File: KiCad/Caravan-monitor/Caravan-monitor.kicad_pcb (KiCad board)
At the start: 2 copper layers, 40 parts, among them IC1 TPS54302DDCR, IC2 STM32L011F4P6TR, IC3 INA500CIDBVR, IC4 TPS54302DDCR, J1 Conn_ARM_JTAG_SWD_20, J2 PJ-059A

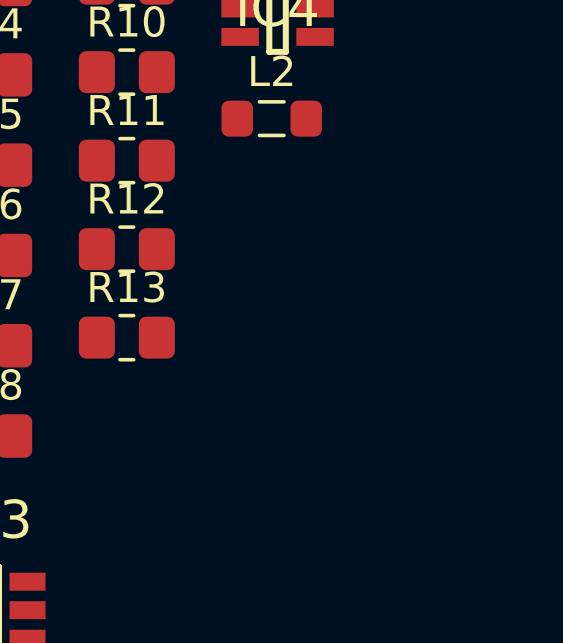
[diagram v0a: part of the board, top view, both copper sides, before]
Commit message: Temperature monitoring schematics
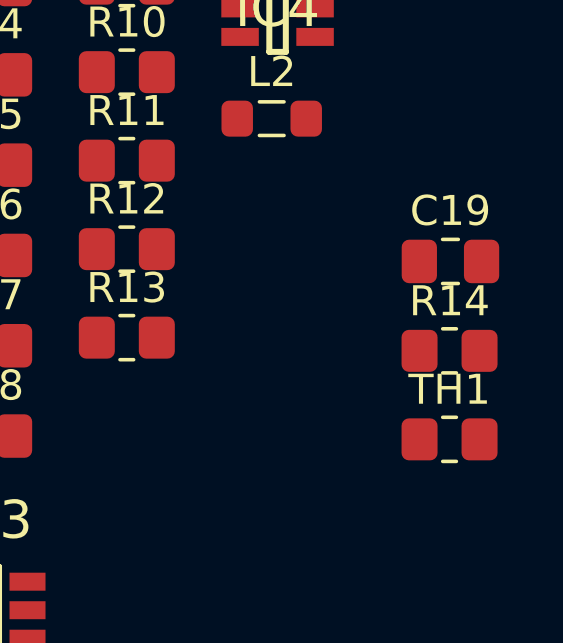
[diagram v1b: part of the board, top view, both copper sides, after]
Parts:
- added C19: 100n, Capacitor_SMD:C_0805_2012Metric_Pad1.18x1.45mm_HandSolder, F.Cu at (125.0, 40.6)
- added R14: 47k, Resistor_SMD:R_0805_2012Metric_Pad1.20x1.40mm_HandSolder, F.Cu at (125.0, 43.5)
- added TH1: Thermistor_NTC, Resistor_SMD:R_0805_2012Metric_Pad1.20x1.40mm_HandSolder, F.Cu at (125.0, 46.5)

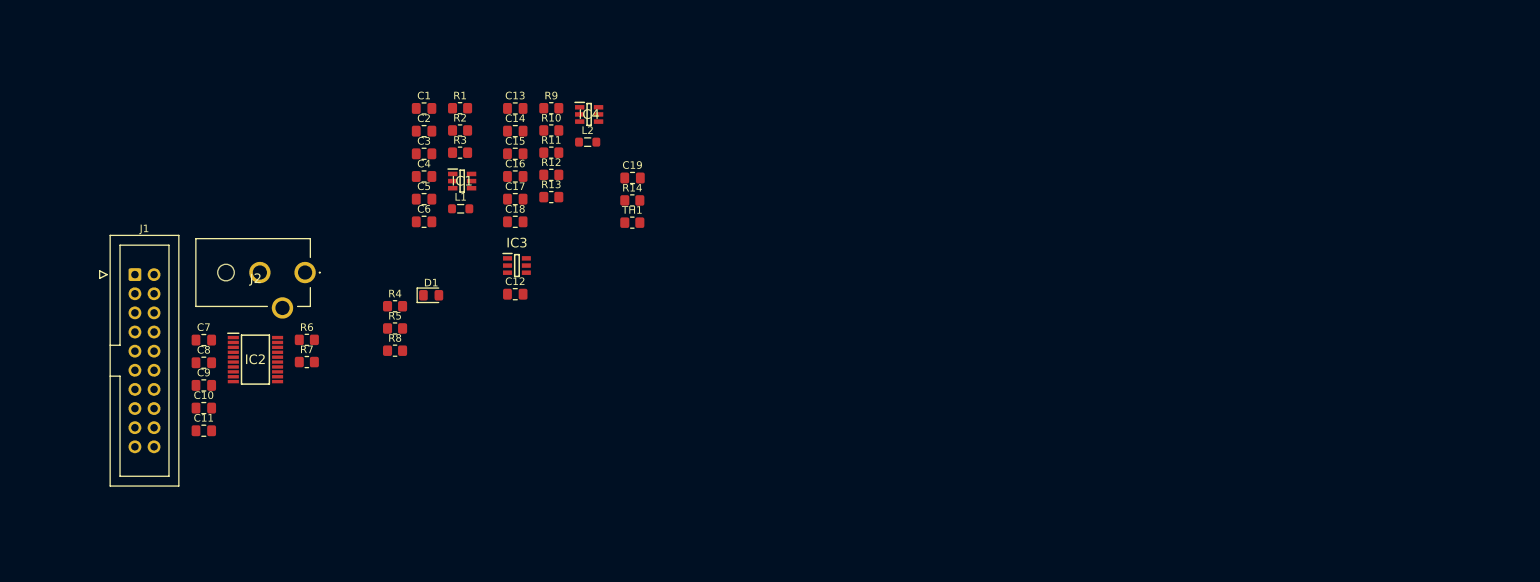
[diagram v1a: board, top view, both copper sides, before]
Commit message: Display schematics
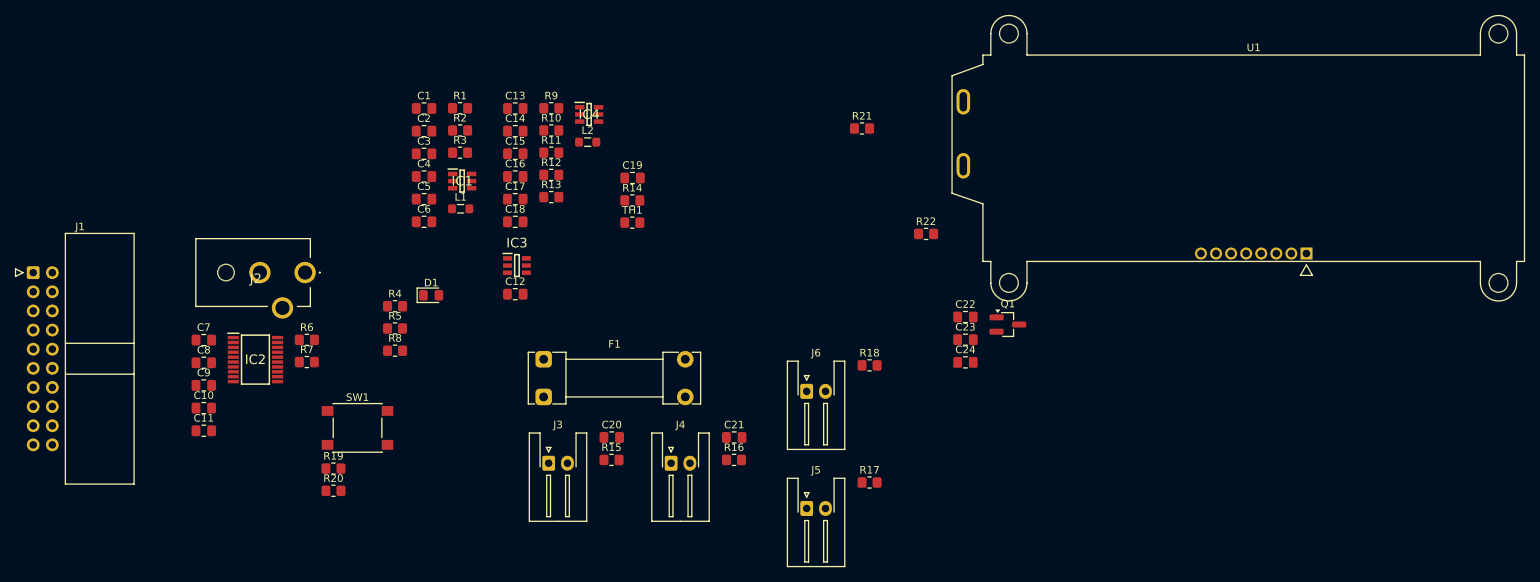
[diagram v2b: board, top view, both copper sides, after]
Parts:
- added C20: 100n, Capacitor_SMD:C_0805_2012Metric_Pad1.18x1.45mm_HandSolder, F.Cu at (122.3, 75.0)
- added C21: 100n, Capacitor_SMD:C_0805_2012Metric_Pad1.18x1.45mm_HandSolder, F.Cu at (138.5, 75.0)
- added C22: 100n, Capacitor_SMD:C_0805_2012Metric_Pad1.18x1.45mm_HandSolder, F.Cu at (169.2, 59.0)
- added C23: 0.47µ, Capacitor_SMD:C_0805_2012Metric_Pad1.18x1.45mm_HandSolder, F.Cu at (169.2, 62.0)
- added C24: 100n, Capacitor_SMD:C_0805_2012Metric_Pad1.18x1.45mm_HandSolder, F.Cu at (169.2, 65.0)
- added F1: 500mA, Fuse:Fuseholder_Clip-5x20mm_Littelfuse_111_Lateral_P18.80x5.00mm_D1.17mm_Horizontal, F.Cu at (113.2, 64.6)
- added J3: Outdoor temp, Connector_JST:JST_XH_S2B-XH-A-1_1x02_P2.50mm_Horizontal, F.Cu at (113.9, 78.4)
- added J4: Coolant temp, Connector_JST:JST_XH_S2B-XH-A-1_1x02_P2.50mm_Horizontal, F.Cu at (130.2, 78.4)
- added J5: Water tank 1, Connector_JST:JST_XH_S2B-XH-A-1_1x02_P2.50mm_Horizontal, F.Cu at (148.2, 84.5)
- added J6: Water tank 2, Connector_JST:JST_XH_S2B-XH-A-1_1x02_P2.50mm_Horizontal, F.Cu at (148.2, 68.9)
- added Q1: 2N7002, Package_TO_SOT_SMD:SOT-23_Handsoldering, F.Cu at (174.9, 60.0)
- added R15: 47k, Resistor_SMD:R_0805_2012Metric_Pad1.20x1.40mm_HandSolder, F.Cu at (122.2, 78.0)
- added R16: 10k, Resistor_SMD:R_0805_2012Metric_Pad1.20x1.40mm_HandSolder, F.Cu at (138.5, 78.0)
- added R17: 10k, Resistor_SMD:R_0805_2012Metric_Pad1.20x1.40mm_HandSolder, F.Cu at (156.5, 81.0)
- added R18: 10k, Resistor_SMD:R_0805_2012Metric_Pad1.20x1.40mm_HandSolder, F.Cu at (156.5, 65.5)
- added R19: 4.7k, Resistor_SMD:R_0805_2012Metric_Pad1.20x1.40mm_HandSolder, F.Cu at (85.3, 79.2)
- added R20: 4.7k, Resistor_SMD:R_0805_2012Metric_Pad1.20x1.40mm_HandSolder, F.Cu at (85.3, 82.1)
- added R21: 10R, Resistor_SMD:R_0805_2012Metric_Pad1.20x1.40mm_HandSolder, F.Cu at (155.5, 34.0)
- added R22: 1k, Resistor_SMD:R_0805_2012Metric_Pad1.20x1.40mm_HandSolder, F.Cu at (164.0, 48.0)
- added SW1: SW_SPST, Button_Switch_SMD:SW_SPST_PTS645, F.Cu at (88.5, 73.8)
- added U1: NHD-C0220BIZ, Display:NHD-C0220BiZ, F.Cu at (207.5, 34.7)
- J1: footprint Connector_IDC:IDC-Header_2x10_P2.54mm_Vertical -> Connector_IDC:IDC-Header_2x10_P2.54mm_Horizontal
- J2: value PJ-059A -> 8-28V input
- moved J1 13.5 mm to (45.5, 53.1)
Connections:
- C19 pad 1: /Indoor temperature/Out -> IndoorTemp
- IC2 pad 10: unconnected-(IC2-PA4-Pad10) -> WaterTank1
- IC2 pad 11: unconnected-(IC2-PA5-Pad11) -> WaterTank2
- IC2 pad 12: unconnected-(IC2-PA6-Pad12) -> DisplayBacklight
- IC2 pad 14: unconnected-(IC2-PB1-Pad14) -> DisplayReset
- IC2 pad 17: unconnected-(IC2-PA9-Pad17) -> SCL
- IC2 pad 18: unconnected-(IC2-PA10-Pad18) -> SDA
- IC2 pad 7: unconnected-(IC2-PA1-Pad7) -> IndoorTemp
- IC2 pad 8: unconnected-(IC2-PA2-Pad8) -> OutdoorTemp
- IC2 pad 9: unconnected-(IC2-PA3-Pad9) -> CoolantTemp
- J2 pad 3: Battery+ -> Net-(F1-Pad2)
- R14 pad 1: /Indoor temperature/3.3V -> 3.3V
- R14 pad 2: /Indoor temperature/Out -> IndoorTemp
- TH1 pad 1: /Indoor temperature/Out -> IndoorTemp

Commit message: Schematics done
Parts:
- removed IC2: STM32L011F4P6TR, SamacSys_Parts:SOP65P640X120-20N
- added C25: 100n, Capacitor_SMD:C_0402_1005Metric_Pad0.74x0.62mm_HandSolder, F.Cu at (69.2, 92.0)
- added C26: 1µ, Capacitor_SMD:C_0402_1005Metric_Pad0.74x0.62mm_HandSolder, F.Cu at (193.7, 71.0)
- added C27: 100n, Capacitor_SMD:C_0402_1005Metric_Pad0.74x0.62mm_HandSolder, F.Cu at (193.7, 74.0)
- added C28: 100n, Capacitor_SMD:C_0402_1005Metric_Pad0.74x0.62mm_HandSolder, F.Cu at (193.7, 77.0)
- added C29: 10p, Capacitor_SMD:C_0402_1005Metric_Pad0.74x0.62mm_HandSolder, F.Cu at (193.7, 80.0)
- added C30: 10p, Capacitor_SMD:C_0402_1005Metric_Pad0.74x0.62mm_HandSolder, F.Cu at (193.7, 83.0)
- added D2: WT1_LED, LED_SMD:LED_0402_1005Metric_Pad0.77x0.64mm_HandSolder, F.Cu at (138.4, 86.0)
- added D3: WT2_LED, LED_SMD:LED_0402_1005Metric_Pad0.77x0.64mm_HandSolder, F.Cu at (138.4, 88.0)
- added FB1: 120R, Inductor_SMD:L_0402_1005Metric_Pad0.77x0.64mm_HandSolder, F.Cu at (198.4, 82.3)
- added J8: STM32 Pins, Connector_PinHeader_2.54mm:PinHeader_2x13_P2.54mm_Horizontal, F.Cu at (148.2, 103.8)
- added R23: 10k, Resistor_SMD:R_0402_1005Metric_Pad0.72x0.64mm_HandSolder, F.Cu at (74.0, 92.0)
- added R24: 1k, Resistor_SMD:R_0402_1005Metric_Pad0.72x0.64mm_HandSolder, F.Cu at (182.5, 84.0)
- added R25: 1k, Resistor_SMD:R_0402_1005Metric_Pad0.72x0.64mm_HandSolder, F.Cu at (134.9, 88.0)
- added SW2: SW_USER, Button_Switch_SMD:SW_SPST_PTS645, F.Cu at (72.4, 86.6)
- added SW3: SW_DPDT_x2, Button_Switch_THT:SW_E-Switch_EG2219_DPDT_Angled, F.Cu at (138.5, 46.2)
- added U2: STM32L010C6Tx, Package_QFP:LQFP-48_7x7mm_P0.5mm, F.Cu at (201.8, 75.2)
- C1, C10, C11, C12, C13, C14, C15, C16, C17, C18, C19, C2, C20, C21, C22, C23, C24, C3, C4, C5, C6, C7, C9: footprint Capacitor_SMD:C_0805_2012Metric_Pad1.18x1.45mm_HandSolder -> Capacitor_SMD:C_0402_1005Metric_Pad0.74x0.62mm_HandSolder
- C8: value 100n -> 10n; footprint Capacitor_SMD:C_0805_2012Metric_Pad1.18x1.45mm_HandSolder -> Capacitor_SMD:C_0402_1005Metric_Pad0.74x0.62mm_HandSolder
- D1: footprint LED_SMD:LED_0805_2012Metric_Pad1.15x1.40mm_HandSolder -> LED_SMD:LED_0402_1005Metric_Pad0.77x0.64mm_HandSolder
- R1, R10, R11, R12, R13, R14, R15, R16, R17, R18, R19, R2, R20, R21, R22, R3, R4, R5, R6, R7, R8, R9, TH1: footprint Resistor_SMD:R_0805_2012Metric_Pad1.20x1.40mm_HandSolder -> Resistor_SMD:R_0402_1005Metric_Pad0.72x0.64mm_HandSolder
- SW1: value SW_SPST -> SW_RESET
- moved J5 59.8 mm to (93.2, 108.2)
- moved J6 58.9 mm to (104.2, 108.2)
- moved J4 57.6 mm to (80.8, 108.2)
- moved J3 54.0 mm to (68.8, 108.2)
- moved R8 47.1 mm to (134.9, 86.0)
- moved J1 29.3 mm to (54.5, 81.0), turned to 180 degrees
- moved J2 27.8 mm to (56.0, 42.2)
- moved U1 15.7 mm to (223.0, 37.2)
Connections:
- net 5V renamed +5V
- C1 pad 1: Battery+ -> +BATT
- C1 pad 2: Battery- -> GND
- C10 pad 1: 3.3V -> +3.3VA
- C10 pad 2: Battery- -> GND
- C11 pad 1: 3.3V -> +3.3V
- C11 pad 2: Battery- -> GND
- C12 pad 2: Battery- -> GND
- C13 pad 1: Battery+ -> +BATT
- C13 pad 2: Battery- -> GND
- C14 pad 1: Battery+ -> +BATT
- C14 pad 2: Battery- -> GND
- C16 pad 2: Battery- -> GND
- C17 pad 2: Battery- -> GND
- C19 pad 2: Battery- -> GND
- C2 pad 1: Battery+ -> +BATT
- C2 pad 2: Battery- -> GND
- C20 pad 2: Battery- -> GND
- C21 pad 2: Battery- -> GND
- C23 pad 1: Battery- -> GND
- C24 pad 1: 3.3V -> +3.3V
- C24 pad 2: Battery- -> GND
- C4 pad 1: 3.3V -> +3.3V
- C4 pad 2: Battery- -> GND
- C5 pad 1: 3.3V -> +3.3V
- C5 pad 2: Battery- -> GND
- C7 pad 1: 3.3V -> +3.3V
- C7 pad 2: Battery- -> GND
- C8 pad 1: 3.3V -> +3.3VA
- C8 pad 2: Battery- -> GND
- C9 pad 1: Battery- -> GND
- D1 pad 1: Battery- -> Net-(D1-K)
- D1 pad 2: Net-(D1-A) -> +3.3V
- F1 pad 1: Battery+ -> Net-(SW3A-B)
- IC1 pad 1: Battery- -> GND
- IC1 pad 3: Battery+ -> +BATT
- IC3 pad 2: Battery- -> GND
- IC3 pad 3: Battery+ -> +BATT
- IC3 pad 4: Battery- -> GND
- IC3 pad 5: Battery- -> GND
- IC4 pad 1: Battery- -> GND
- IC4 pad 3: Battery+ -> +BATT
- J1 pad 10: Battery- -> GND
- J1 pad 12: Battery- -> GND
- J1 pad 14: Battery- -> GND
- J1 pad 16: Battery- -> GND
- J1 pad 18: Battery- -> GND
- J1 pad 2: 3.3V -> +3.3V
- J1 pad 20: Battery- -> GND
- J1 pad 4: Battery- -> GND
- J1 pad 6: Battery- -> GND
- J1 pad 8: Battery- -> GND
- J2 pad 2: Battery- -> GND
- J3 pad 2: Battery- -> GND
- J4 pad 2: Battery- -> GND
- J5 pad 2: Battery- -> GND
- J6 pad 2: Battery- -> GND
- L1 pad 2: 3.3V -> +3.3V
- Q1 pad 2: Battery- -> GND
- R1 pad 1: Battery+ -> +BATT
- R10 pad 2: Battery- -> GND
- R12 pad 1: Battery+ -> +BATT
- R13 pad 2: Battery- -> GND
- R14 pad 1: 3.3V -> +3.3V
- R15 pad 1: 3.3V -> +3.3V
- R16 pad 1: 3.3V -> +3.3V
- R17 pad 1: 3.3V -> +3.3V
- R18 pad 1: 3.3V -> +3.3V
- R19 pad 1: 3.3V -> +3.3V
- R19 pad 2: SDA -> SCL
- R2 pad 2: Battery- -> GND
- R20 pad 1: 3.3V -> +3.3V
- R20 pad 2: SCL -> SDA
- R21 pad 1: 3.3V -> +3.3V
- R3 pad 1: 3.3V -> +3.3V
- R5 pad 2: Battery- -> GND
- R6 pad 1: Battery- -> GND
- R6 pad 2: Net-(IC2-PB9-BOOT0) -> /BOOT0
- R7 pad 1: 3.3V -> +3.3V
- R8 pad 1: 3.3V -> Net-(D3-K)
- R8 pad 2: Net-(D1-A) -> GND
- SW1 pad 2: Battery- -> GND
- TH1 pad 2: Battery- -> GND
- U1 pad 4: Battery- -> GND
- U1 pad 5: 3.3V -> +3.3V
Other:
- board text added: "8-28V"
- board text added: "ST-LINK"

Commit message: 3.3V and 5V PSU layout done
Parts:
- removed R7: 10k, Resistor_SMD:R_0402_1005Metric_Pad0.72x0.64mm_HandSolder
- removed SW1: SW_RESET, Button_Switch_SMD:SW_SPST_PTS645
- moved C11 144.0 mm to (203.9, 122.0)
- moved C8 144.0 mm to (203.9, 113.0)
- moved C9 144.0 mm to (203.9, 116.0)
- moved C10 144.0 mm to (203.9, 119.0)
- moved C7 144.0 mm to (203.9, 110.0)
- moved R24 132.7 mm to (61.5, 29.5), turned to -90 degrees
- moved C12 129.3 mm to (232.0, 97.3)
- moved C19 129.3 mm to (247.6, 81.8)
- moved IC3 129.3 mm to (232.2, 93.5)
- moved R14 129.3 mm to (247.6, 84.8)
- moved R21 129.3 mm to (278.1, 75.3)
- moved TH1 129.3 mm to (247.6, 87.8)
- moved U2 129.3 mm to (72.5, 77.5)
- moved C23 110.0 mm to (270.7, 104.5)
- moved C24 110.0 mm to (270.7, 107.5)
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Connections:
- C9 pad 2: NRST -> /NRST
- J1 pad 15: NRST -> unconnected-(J1-~{SRST}-Pad15)
- U2 pad 7: NRST -> /NRST
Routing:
- net GND: track 0.00 -> 53.9 mm, vias 0 -> 10
- net +BATT: track 0.00 -> 30.5 mm
- net Net-(C6-Pad1): track 0.00 -> 19.3 mm
- net Net-(SW3A-B): track 0.00 -> 17.7 mm
- net Net-(F1-Pad2): track 0.00 -> 13.5 mm
- net Net-(IC4-EN): track 0.00 -> 11.8 mm
- net Net-(IC1-EN): track 0.00 -> 11.5 mm
- net Net-(IC4-SW): track 0.00 -> 8.20 mm, vias 0 -> 2
- net Net-(IC1-SW): track 0.00 -> 7.89 mm, vias 0 -> 2
- net Net-(IC1-BOOT): track 0.00 -> 7.50 mm, vias 0 -> 2
- net +3.3V: track 0.00 -> 7.43 mm
- net Net-(IC4-BOOT): track 0.00 -> 6.86 mm, vias 0 -> 2
- net Net-(IC1-FB): track 0.00 -> 6.79 mm
- net +5V: track 0.00 -> 6.73 mm
- net Net-(IC4-FB): track 0.00 -> 6.31 mm
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
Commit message: PCB Designed
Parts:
- removed C13: 10µ, Capacitor_SMD:C_0402_1005Metric_Pad0.74x0.62mm_HandSolder
- removed C14, C15: 0.1µ, Capacitor_SMD:C_0402_1005Metric_Pad0.74x0.62mm_HandSolder
- removed C16, C17: 22µ, Capacitor_SMD:C_0402_1005Metric_Pad0.74x0.62mm_HandSolder
- removed C18: 75p, Capacitor_SMD:C_0402_1005Metric_Pad0.74x0.62mm_HandSolder
- removed IC4: TPS54302DDCR, SamacSys_Parts:SOT95P280X110-6N
- removed J8: STM32 Pins, Connector_PinHeader_2.54mm:PinHeader_2x13_P2.54mm_Horizontal
- removed L2: 10µ, Inductor_SMD:L_0805_2012Metric_Pad1.05x1.20mm_HandSolder
- removed R10: 13.3k, Resistor_SMD:R_0402_1005Metric_Pad0.72x0.64mm_HandSolder
- removed R11: 49.9, Resistor_SMD:R_0402_1005Metric_Pad0.72x0.64mm_HandSolder
- removed R12: 511k, Resistor_SMD:R_0402_1005Metric_Pad0.72x0.64mm_HandSolder
- removed R13: 105k, Resistor_SMD:R_0402_1005Metric_Pad0.72x0.64mm_HandSolder
- removed R9: 100k, Resistor_SMD:R_0402_1005Metric_Pad0.72x0.64mm_HandSolder
- added Y1: 16MHz, Package_LGA:VLGA-4_2x2.5mm_P1.65mm, F.Cu at (64.6, 55.2)
- C22, C23, C24, R21: moved to B.Cu
- moved IC3 193.4 mm to (43.8, 50.0)
- moved C12 193.1 mm to (45.5, 47.5)
- moved R17 181.3 mm to (77.6, 106.2)
- moved D2 175.5 mm to (76.5, 64.5), turned to 180 degrees
- moved R21 172.7 mm to (105.5, 81.1), turned to 90 degrees
- moved D3 172.6 mm to (76.5, 75.0), turned to 180 degrees
- moved R16 172.0 mm to (68.6, 106.2)
- moved R18 171.7 mm to (86.3, 106.2)
- moved C23 171.2 mm to (101.0, 82.1), turned to 90 degrees
- moved R25 170.8 mm to (78.9, 64.5)
- moved C21 169.5 mm to (70.9, 106.0)
- moved C24 168.0 mm to (104.5, 83.4), turned to -90 degrees
- moved R8 166.3 mm to (79.0, 75.0)
- moved R14 165.4 mm to (87.0, 45.0)
- moved R15 164.8 mm to (59.6, 106.2)
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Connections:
- net Net-(Q1-D) renamed /Display/BL_Cathode
- net Net-(U1-A) renamed /Display/BL_Anode
- C12 pad 1: +5V -> +3.3V
- IC3 pad 6: +5V -> +3.3V
- U2 pad 1: PC0 -> unconnected-(U2-PC0-Pad1)
- U2 pad 12: Net-(J8-Pin_3) -> unconnected-(U2-PA2-Pad12)
- U2 pad 13: Net-(J8-Pin_4) -> unconnected-(U2-PA3-Pad13)
- U2 pad 14: Net-(J8-Pin_5) -> unconnected-(U2-PA4-Pad14)
- U2 pad 15: Net-(J8-Pin_6) -> unconnected-(U2-PA5-Pad15)
- U2 pad 16: Net-(J8-Pin_7) -> unconnected-(U2-PA6-Pad16)
- U2 pad 17: Net-(J8-Pin_8) -> unconnected-(U2-PA7-Pad17)
- U2 pad 18: PB0 -> unconnected-(U2-PB0-Pad18)
- U2 pad 19: PB1 -> unconnected-(U2-PB1-Pad19)
- U2 pad 2: PC13 -> unconnected-(U2-PC13-Pad2)
- U2 pad 20: PB2 -> unconnected-(U2-PB2-Pad20)
- U2 pad 29: Net-(J8-Pin_9) -> unconnected-(U2-PA8-Pad29)
- U2 pad 3: PC14 -> unconnected-(U2-PC14-Pad3)
- U2 pad 32: Net-(J8-Pin_10) -> unconnected-(U2-PA11-Pad32)
- U2 pad 33: Net-(J8-Pin_11) -> unconnected-(U2-PA12-Pad33)
- U2 pad 38: Net-(J8-Pin_12) -> unconnected-(U2-PA15-Pad38)
- U2 pad 39: PB3 -> unconnected-(U2-PB3-Pad39)
- U2 pad 4: PC15 -> unconnected-(U2-PC15-Pad4)
- U2 pad 40: PB4 -> unconnected-(U2-PB4-Pad40)
- U2 pad 41: PB5 -> unconnected-(U2-PB5-Pad41)
- U2 pad 42: PB6 -> unconnected-(U2-PB6-Pad42)
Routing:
- net GND: track 53.9 -> 396.1 mm, vias 10 -> 7
- net +3.3V: track 7.43 -> 263.4 mm
- net WaterTank2: track 0.00 -> 98.6 mm, vias 0 -> 1
- net OutdoorTemp: track 0.00 -> 70.6 mm, vias 0 -> 1
- net CoolantTemp: track 0.00 -> 67.7 mm, vias 0 -> 1
- net SWDIO: track 0.00 -> 67.2 mm, vias 0 -> 1
- net SWCLK: track 0.00 -> 65.4 mm, vias 0 -> 1
- net WaterTank1: track 0.00 -> 64.3 mm, vias 0 -> 1
- net DisplayReset: track 0.00 -> 59.6 mm, vias 0 -> 1
- net SDA: track 0.00 -> 59.4 mm, vias 0 -> 3
- net SCL: track 0.00 -> 55.0 mm, vias 0 -> 1
- net Net-(SW2-B): track 0.00 -> 46.8 mm, vias 0 -> 2
- net /Display/BL_Cathode: track 0.00 -> 39.9 mm
- net /Display/BL_Anode: track 0.00 -> 39.3 mm
- net BatteryVoltage: track 0.00 -> 37.8 mm, vias 0 -> 2
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- added copper zone on B.Cu, net GND
- added copper zone on F.Cu, net GND
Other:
- board outline added: 102.5 x 80 mm
- board text added: "12V Battery"
- board text added: "500mA"
- board text added: "Coolant temp"
- board text added: "Outdoor temp"
- board text added: "Water tank 1"
- board text added: "Water tank 1 LED"
- board text added: "Water tank 2"
- board text added: "Water tank 2 LED"
- board text removed: "8-28V"

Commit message: Version 0.1 complete
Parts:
- removed C29, C30: 10p, Capacitor_SMD:C_0402_1005Metric_Pad0.74x0.62mm_HandSolder
- removed Y1: 16MHz, Package_LGA:VLGA-4_2x2.5mm_P1.65mm
- added G***: LOGO, LOGO, B.Cu at (113.0, 106.5)
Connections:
- U2 pad 5: /OSC_IN -> unconnected-(U2-PH0-Pad5)
- U2 pad 6: /OSC_OUT -> unconnected-(U2-PH1-Pad6)
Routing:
- net GND: track 396.1 -> 381.1 mm
- net /OSC_IN: track 9.45 -> 0.00 mm
- net /OSC_OUT: track 8.09 -> 0.00 mm
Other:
- board text added: "V0.1 5/26"
- board text added: "https://github.com/peltonenmikko/Caravan-Monitor"
